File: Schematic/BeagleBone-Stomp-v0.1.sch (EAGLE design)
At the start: 8 parts, among them U1 MSP430G2553_RHB_32, U2 TLV320AIC3120_RHB_32

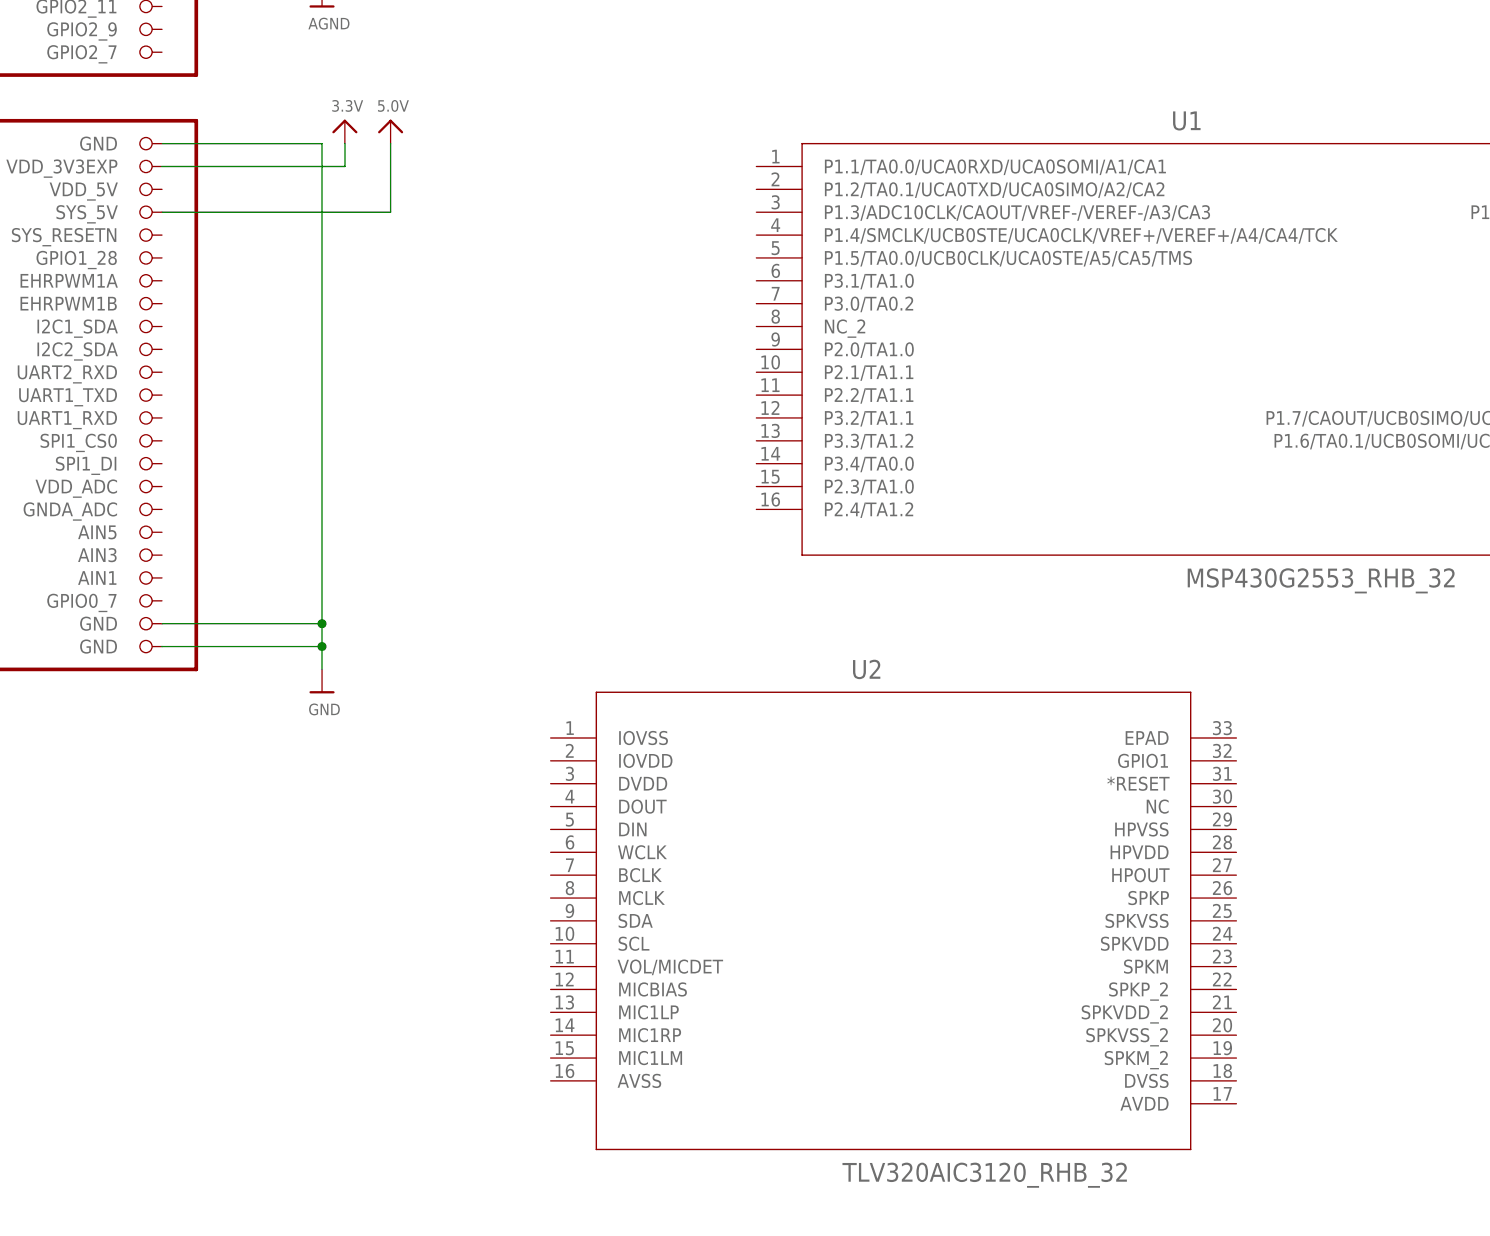
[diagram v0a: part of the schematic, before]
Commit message: connected a few of the pins in the design.
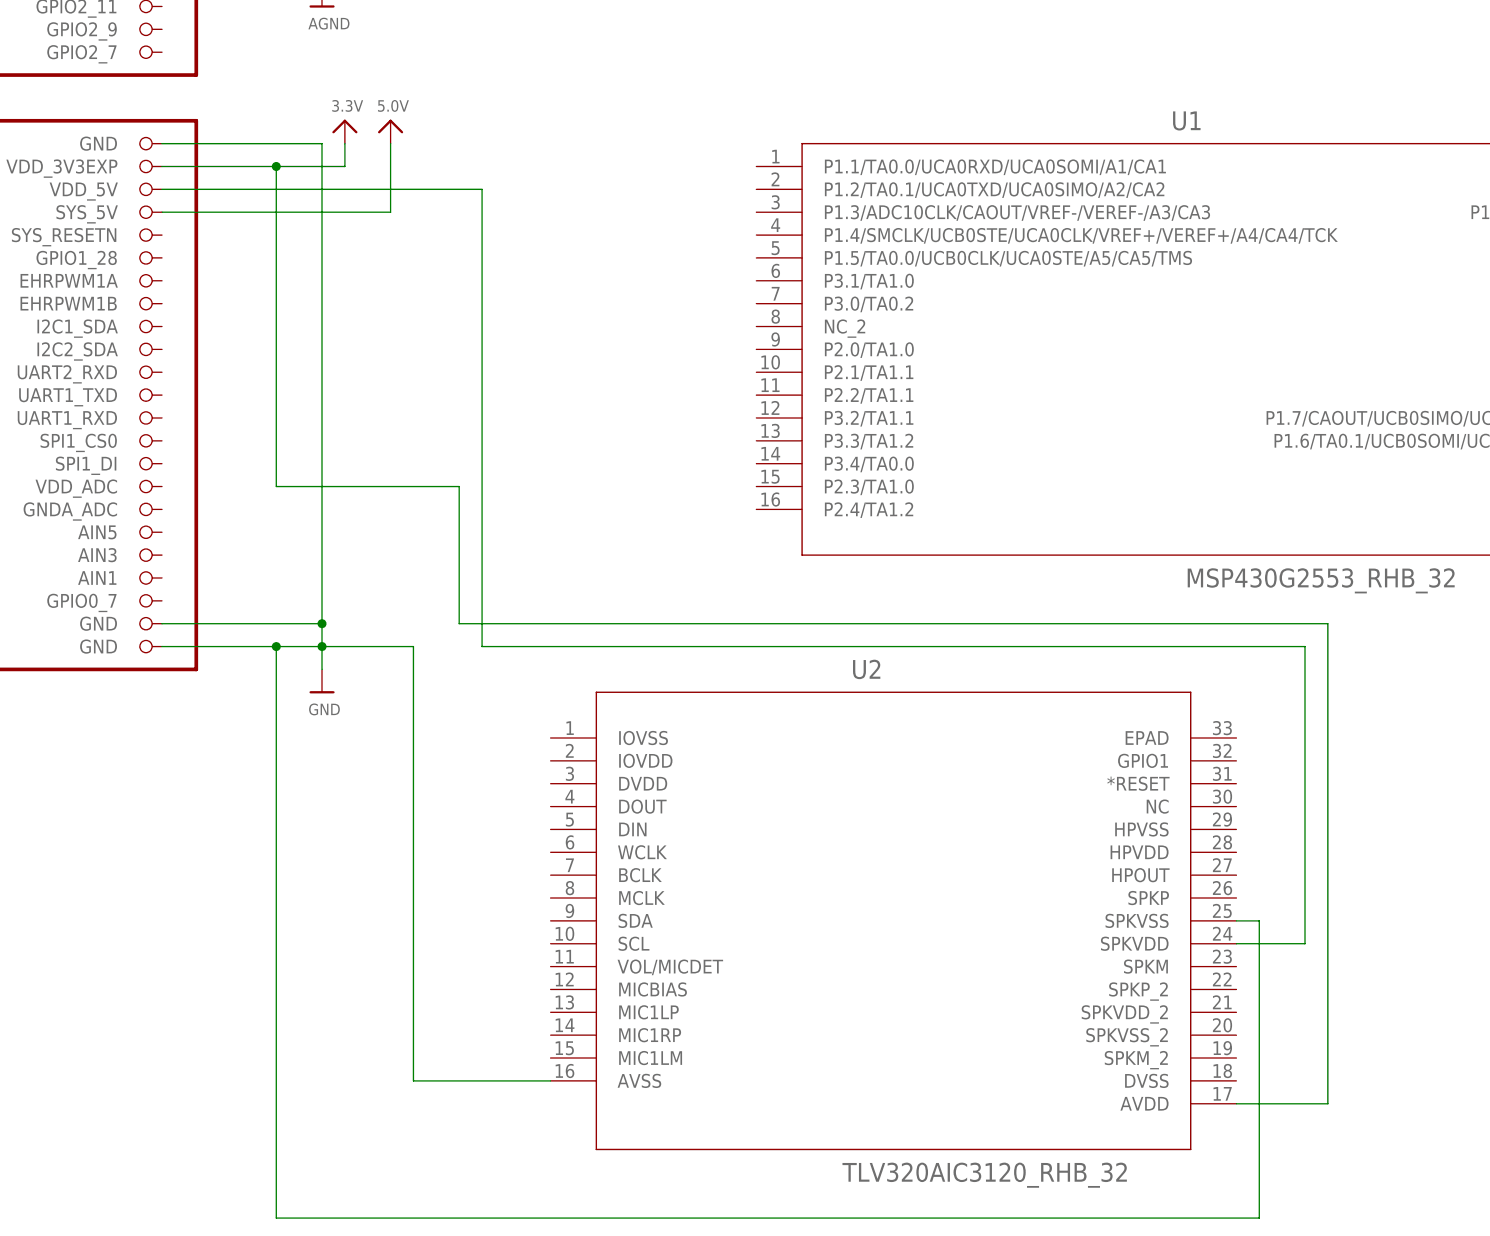
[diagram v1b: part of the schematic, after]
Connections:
- new net N$1: U$2.VDD_5V@2, U2.SPKVDD
- net 3.3V: now also U2.AVDD
- net GND: now also U2.AVSS, U2.SPKVSS
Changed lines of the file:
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@@
 <pinref part="U$11" gate="G$1" pin="3.3V"/>
 <pinref part="U$2" gate="G$1" pin="VDD_3V3EXP@2"/>
-<wire x1="208.28" y1="124.46" x2="228.6" y2="124.46" width="0.1524" layer="91"/>
+<wire x1="208.28" y1="124.46" x2="220.98" y2="124.46" width="0.1524" layer="91"/>
+<pinref part="U2" gate="A" pin="AVDD"/>
+<wire x1="220.98" y1="124.46" x2="228.6" y2="124.46" width="0.1524" layer="91"/>
+<wire x1="241.3" y1="88.9" x2="241.3" y2="73.66" width="0.1524" layer="91"/>
+<wire x1="241.3" y1="73.66" x2="337.82" y2="73.66" width="0.1524" layer="91"/>
+<wire x1="337.82" y1="73.66" x2="337.82" y2="20.32" width="0.1524" layer="91"/>
+<wire x1="337.82" y1="20.32" x2="327.66" y2="20.32" width="0.1524" layer="91"/>
+<wire x1="241.3" y1="88.9" x2="220.98" y2="88.9" width="0.1524" layer="91"/>
+<wire x1="220.98" y1="88.9" x2="220.98" y2="124.46" width="0.1524" layer="91"/>
+<junction x="220.98" y="124.46"/>
 </segment>
 <segment>
@@
 <pinref part="U$2" gate="G$1" pin="GND@6"/>
 <wire x1="226.06" y1="68.58" x2="226.06" y2="71.12" width="0.1524" layer="91"/>
-<wire x1="226.06" y1="71.12" x2="208.28" y2="71.12" width="0.1524" layer="91"/>
+<wire x1="226.06" y1="71.12" x2="220.98" y2="71.12" width="0.1524" layer="91"/>
 <pinref part="U$2" gate="G$1" pin="GND@5"/>
+<wire x1="220.98" y1="71.12" x2="208.28" y2="71.12" width="0.1524" layer="91"/>
 <wire x1="226.06" y1="71.12" x2="226.06" y2="73.66" width="0.1524" layer="91"/>
 <wire x1="208.28" y1="73.66" x2="226.06" y2="73.66" width="0.1524" layer="91"/>
@@
 <junction x="226.06" y="73.66"/>
 <junction x="226.06" y="71.12"/>
+<pinref part="U2" gate="A" pin="AVSS"/>
+<wire x1="236.22" y1="22.86" x2="251.46" y2="22.86" width="0.1524" layer="91"/>
+<wire x1="226.06" y1="71.12" x2="236.22" y2="71.12" width="0.1524" layer="91"/>
+<wire x1="236.22" y1="71.12" x2="236.22" y2="22.86" width="0.1524" layer="91"/>
+<pinref part="U2" gate="A" pin="SPKVSS"/>
+<wire x1="327.66" y1="40.64" x2="330.2" y2="40.64" width="0.1524" layer="91"/>
+<wire x1="330.2" y1="40.64" x2="330.2" y2="7.62" width="0.1524" layer="91"/>
+<wire x1="330.2" y1="7.62" x2="220.98" y2="7.62" width="0.1524" layer="91"/>
+<wire x1="220.98" y1="7.62" x2="220.98" y2="71.12" width="0.1524" layer="91"/>
+<junction x="220.98" y="71.12"/>
 </segment>
 </net>
@@
 </segment>
 </net>
+<net name="N$1" class="0">
+<segment>
+<pinref part="U2" gate="A" pin="SPKVDD"/>
+<wire x1="327.66" y1="38.1" x2="335.28" y2="38.1" width="0.1524" layer="91"/>
+<wire x1="335.28" y1="38.1" x2="335.28" y2="71.12" width="0.1524" layer="91"/>
+<wire x1="335.28" y1="71.12" x2="243.84" y2="71.12" width="0.1524" layer="91"/>
+<wire x1="243.84" y1="71.12" x2="243.84" y2="121.92" width="0.1524" layer="91"/>
+<pinref part="U$2" gate="G$1" pin="VDD_5V@2"/>
+<wire x1="243.84" y1="121.92" x2="208.28" y2="121.92" width="0.1524" layer="91"/>
+</segment>
+</net>

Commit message: Making some changes
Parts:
- added C1, C3, C4: 0.1u, microbuilder:CAP_CERAMIC0402
- added FB1: (no value), microbuilder:FERRITE_0402
- added R1: 28k, microbuilder:RESISTOR0402
- added R2: 56.2k, microbuilder:RESISTOR0402
- added U3: TPS73701_DRB_8, bone:TPS73701_DRB_8
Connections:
- new net 1.8V: C4.P$2, R1.1, U2.DVDD, U3.OUT
- net 3.3V: now also C1.P$1, U1.DVCC, U2.IOVDD, U3.EN, U3.IN
- net 5.0V: now also C3.P$1, U2.SPKVDD
- net AGND: now also FB1.P$1, U2.AVSS, U2.EPAD
- net GND: now also C1.P$2, C3.P$2, FB1.P$2, R2.1, U1.DVSS, U2.DVSS, U2.IOVSS, U3.EPAD, U3.GND; no longer U2.AVSS
- net N$1: now also C4.P$1, R1.2, R2.2, U3.NR/FB; no longer U$2.VDD_5V@2, U2.SPKVDD
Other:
- moved on the sheet: JP1, JP2, JP3, U$1, U$2, U$7, U1, U2

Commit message: Adding MSP430 connections
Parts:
- added C10, C11, C12, C2, C7, C9: 10u, microbuilder:CAP_CERAMIC0805
- added C13, C14, C5, C6, C8: 0.1u, microbuilder:CAP_CERAMIC0402
- added GND, RST, SPKM, SPKP, TST, VCC: WIREPAD2,15/1,0, wirepad:WIREPAD2,15/1,0
- added R10, R11, R12, R13, R14, R15, R16: 10k, microbuilder:RESISTOR0402
- added R3, R4, R5, R6, R7, R8, R9: 470, microbuilder:RESISTOR0402
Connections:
- new net N$10: C11.P$1, U2.MIC1RP
- new net N$11: C12.P$1, U2.MIC1LP
- new net N$12: JP2.6, U1.P1.0/TA0CLK/ACLK/A0/CA0
- new net N$13: JP2.14, R9.2
- new net N$14: JP2.15, R8.2
- new net N$15: JP2.16, R7.2
- new net N$16: JP2.17, R6.2
- new net N$17: JP2.1, U1.P1.5/TA0.0/UCB0CLK/UCA0STE/A5/CA5/TMS
- new net N$18: JP2.2, U1.P1.4/SMCLK/UCB0STE/UCA0CLK/VREF+/VEREF+/A4/CA4/TCK
- new net N$19: JP2.4, U1.P1.2/TA0.1/UCA0TXD/UCA0SIMO/A2/CA2
- new net N$20: JP2.5, U1.P1.1/TA0.0/UCA0RXD/UCA0SOMI/A1/CA1
- new net N$21: JP2.3, U1.P1.3/ADC10CLK/CAOUT/VREF-/VEREF-/A3/CA3
- new net N$22: JP2.18, R5.2
- new net N$23: JP2.19, R4.2
- new net N$24: JP2.20, R3.2
- new net N$25: JP1.19, U1.P2.3/TA1.0
- new net N$26: JP1.20, U1.P3.4/TA0.0
- new net N$27: JP1.14, U1.P3.7/TA1CLK/CAOUT
- new net N$28: JP1.15, U1.P3.6/TA0.2
- new net N$29: JP1.16, U1.P3.5/TA0.1
- new net N$3: SPKM.P, U2.SPKM
- new net N$30: JP1.17, U1.P2.5/TA1.2
- new net N$31: JP1.18, U1.P2.4/TA1.2
- new net N$32: TST.P, U1.TEST/SBWTCK
- new net N$33: RST.P, U1.*RST/NMI/SBWTDIO
- new net N$34: JP2.7, R16.2, U1.P3.1/TA1.0
- new net N$35: JP2.8, R15.2, U1.P3.0/TA0.2
- new net N$36: JP2.9, R14.2, U1.P2.0/TA1.0
- new net N$37: JP2.10, R13.2, U1.P2.1/TA1.1
- new net N$38: JP2.11, R12.2, U1.P2.2/TA1.1
- new net N$39: JP2.12, R11.2, U1.P3.2/TA1.1
- new net N$4: SPKP.P, U2.SPKP
- new net N$40: JP2.13, R10.2, U1.P3.3/TA1.2
- new net N$5: C10.P$1, U2.HPOUT
- new net N$6: C10.P$2, U$7.T
- new net N$7: C9.P$2, U$7.S
- new net N$8: C12.P$2, U$1.S
- new net N$9: C11.P$2, U$1.T
- net 1.8V: now also C5.P$1
- net 3.3V: now also C13.P$1, C14.P$1, C2.P$1, C6.P$1, C7.P$1, C8.P$1, JP3.1, JP3.2, JP3.3, JP3.4, JP3.5, JP3.6, R10.1, R11.1, R12.1, R13.1, R14.1, R15.1, R16.1, R3.1, R4.1, R5.1, R6.1, R7.1, R8.1, R9.1, U1.AVCC, U2.HPVDD, VCC.P
- net AGND: now also C13.P$2, C2.P$2, C6.P$2, U1.AVSS, U1.EPAD
- net GND: now also C14.P$2, C5.P$2, C7.P$2, C8.P$2, C9.P$1, GND.P, JP1.1, JP1.10, JP1.11, JP1.12, JP1.13, JP1.2, JP1.3, JP1.4, JP1.5, JP1.6, JP1.7, JP1.8, JP1.9, U2.HPVSS
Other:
- moved on the sheet: C1, C3, C4, JP1, JP2, JP3, R1, R2, U$1, U$2, U$7, U1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

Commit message: Adding crystal and a couple caps. Also added codec connections
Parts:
- removed C11: 10u, microbuilder:CAP_CERAMIC0805
- added C15, C16: 22u, microbuilder:CAP_CERAMIC0805
- added C17: 0.1u, microbuilder:CAP_CERAMIC0402
- added C18, C19: 10u, microbuilder:CAP_CERAMIC0805
- added R17, R18: 4.7k, microbuilder:RESISTOR0402
- added U$20: FXO-HC735-12, bone:FXO-HC735-12
- C10: value 10u -> 47u
- C12: value 10u -> 0.1u; device microbuilder:CAP_CERAMIC0805 -> microbuilder:CAP_CERAMIC0402
- C9: value 10u -> 0.01u; device microbuilder:CAP_CERAMIC0805 -> microbuilder:CAP_CERAMIC0402
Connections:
- removed net N$7 (its old number): C9.P$2, U$7.S
- new net N$24: U$2.GPIO3_21, U2.DIN
- new net N$41: U$2.SPI1_DO, U2.WCLK
- new net N$42: U$2.SPI1_SCLK, U2.BCLK
- new net N$43: C16.P$1, C17.P$1, U2.SPKVDD_2
- new net N$44: R18.1, U$2.I2C2_SDA, U1.P1.7/CAOUT/UCB0SIMO/UCB0SDA/A7/CA7/TDO/TDI, U2.SDA
- new net N$45: U$2.SYS_RESETN, U2.*RESET
- new net N$46: R17.1, U$2.I2C2_SCL, U1.P1.6/TA0.1/UCB0SOMI/UCB0SCL/A6/CA6/TDI/TCLK, U2.SCL
- net 1.8V: now also C18.P$1
- net 3.3V: now also C19.P$1, C9.P$1, R17.2, R18.2, U$20.VDD
- net 5.0V: now also C15.P$1
- net AGND: now also C15.P$2, C16.P$2, C17.P$2, C3.P$2, C7.P$2, C8.P$2, U$1.S, U$7.S, U2.HPVSS, U2.SPKVSS, U2.SPKVSS_2
- net GND: now also C18.P$2, C19.P$2, C9.P$2, U$20.GND; no longer C3.P$2, C7.P$2, C8.P$2, C9.P$1, U2.HPVSS, U2.SPKVSS
- net N$10: now also C12.P$2; no longer C11.P$1
- net N$11: now also U$2.SPI1_CS0, U2.DOUT; no longer C12.P$1, U2.MIC1LP
- net N$3: now also U2.SPKM_2
- net N$4: now also U2.SPKP_2
- net N$8: now also U$20.OUT, U2.MCLK; no longer C12.P$2, U$1.S
- net N$9: now also C12.P$1; no longer C11.P$2
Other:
- moved on the sheet: C12, C9
